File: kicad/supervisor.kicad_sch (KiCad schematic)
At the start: 63 parts, among them J1 USB-C, J2 FPGA JTAG, J51 CTRL SWD, J52 PZ254V-11-02P, SW1 CTRL BOOT, U18 CH224K, U20 SN74CB3Q3384APWR, U7 RP2350B, U8 W25Q32JVZP, Y1 12MHz ABM8-272-T3

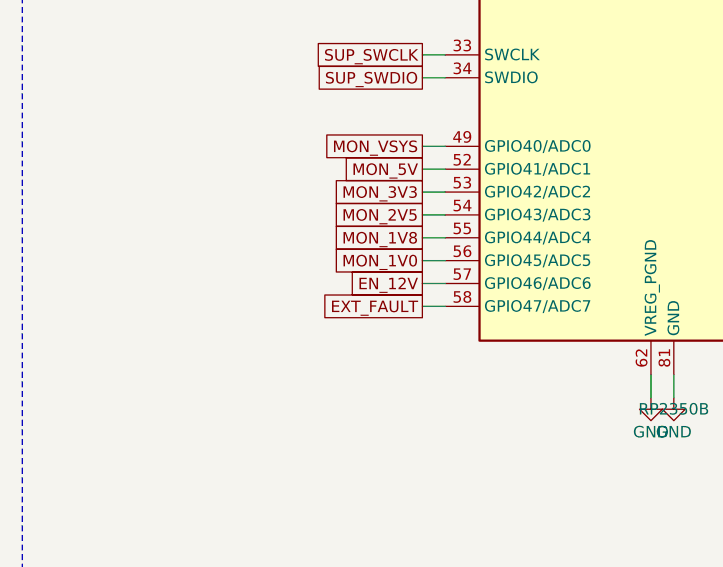
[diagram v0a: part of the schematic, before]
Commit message: Through-hole extension headers, AUX supply rework, and board state before rev A cleanup
J3/J5 become single 2x32 through-hole bodies with IO IO GND rows and a long
grounded key post per zone. Power sheet reworked around the AUX rail.
Decoupling moved off B.Cu. New footprints, 3D models and check scripts.
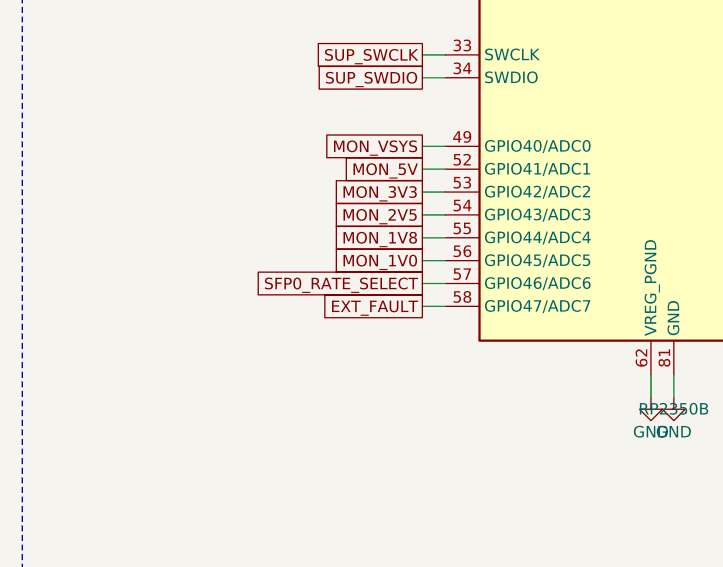
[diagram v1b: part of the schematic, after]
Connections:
- net EN_12V renamed SFP0_RATE_SELECT

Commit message: Fast Links out, Network in: RTL8211FD-CG on RGMII, ETH jack, LINK P and LINK Q
The two SFP ports, their cages, the 125 MHz oscillator, the power gate and
the I2C switch leave the design, and with them the SFP nets on the board
controller (GPIO32-39 and 46 are spare, GPIO14/31 carry the status expander's
I2C). Both GTP quads stay powered per UG482 with grounded RX and one RCAL
each.

A Network sheet replaces them: an RTL8211FD-CG gigabit PHY on RGMII at 2.5 V
with its straps, reset, interrupt, MDIO pull-up, crystal and jack LEDs wired
from the datasheet rev 1.7 tables, a HanRun HR911130A 1000Base-T magjack,
and two plain shielded 8P8C jacks that carry eight DC-coupled LVDS_25 pairs
from bank 16 with ESD arrays at the jacks. The five new parts came in through
easyeda2kicad; two footprints the importer had shared with other parts got
their own copies, and the jacks' mounting holes are NPTH.

Bank 16 moves to +2V5 and tools/alloc.py allocates it shallowest-first with
the PHY receive clock on an MRCC ball and the two link receive clocks on
clock-capable pairs; both 5 V buses and the PHY control pins live in bank 13;
banks 13, 14 and 16 are depth sorted. Escape depth >= 7 drops from 58 to 50
balls. Docs: ref/network.md and ref/link-ports.md are new; the SFP pages are
gone; status LEDs, user manual, keep-outs and import checklist follow.
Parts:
- added C182: 100nF, Capacitor_SMD:C_0402_1005Metric, symbol Device:C
- added D10, D11, D9: F.0603.00025/P2-0603G1TS2-06T-002, EasyEDA:LED0603-RD_GREEN, symbol EasyEDA:F.0603.00025_P2-0603G1TS2-06T-002
- added R128, R129, R130: 1k, Resistor_SMD:R_0402_1005Metric, symbol Device:R
- added R37, R38, R45: 4.7k, Resistor_SMD:R_0402_1005Metric, symbol Device:R
- added U17: PCF8574T_3,518, EasyEDA:SOIC-16_L10.3-W7.5-P1.27-LS10.3-BL, symbol EasyEDA:PCF8574T_3,518
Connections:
- net +3V3: now also C182.1, R128.1, R129.1, R130.1, R37.1, R38.1, R45.1, U17.16 (VDD), U17.3 (A2)
- net GND: now also C182.2, U17.1 (A0), U17.2 (A1), U17.8 (VSS)
- net SFP0_LOS: no longer names the net of U7.44 (GPIO35)
- net SFP0_MOD_ABS: no longer names the net of U7.40 (GPIO32)
- net SFP0_RATE_SELECT: no longer names the net of U7.57 (GPIO46/ADC6)
- net SFP0_TX_DIS: no longer names the net of U7.42 (GPIO33)
- net SFP0_TX_FAULT: no longer names the net of U7.43 (GPIO34)
- net SFP1_LOS: no longer names the net of U7.48 (GPIO39)
- net SFP1_MOD_ABS: no longer names the net of U7.45 (GPIO36)
- net SFP1_TX_DIS: no longer names the net of U7.46 (GPIO37)
- net SFP1_TX_FAULT: no longer names the net of U7.47 (GPIO38)
- net SFP_SCL renamed SUP_SCL
- net SUP_SCL: now also R37.2, U17.14 (SCL)
- net SFP_SDA renamed SUP_SDA
- net SUP_SDA: now also R38.2, U17.15 (SDA)
- new net CORE_1V0_GOOD: U17.7 (P3)
- new net LED_HEARTBEAT_A: D9.2 (A), R128.2
- new net LED_HEARTBEAT_N: D9.1 (C), U17.4 (P0)
- new net LED_USER1_A: D10.2 (A), R129.2
- new net LED_USER1_N: D10.1 (C), U17.5 (P1)
- new net LED_USER2_A: D11.2 (A), R130.2
- new net LED_USER2_N: D11.1 (C), U17.6 (P2)
- new net SUP_EXP_INT: R45.2, U17.13 (~{INT})
- no-connect marks 18 -> 31
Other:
- note added: "board status LEDs"
- note added: "status expander"
- moved on the sheet: C136, C137, C138, D6, D7, J1, J2, J51, J52, R11, R12, R13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

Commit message: Explain the remaining four sheets: power, memory, board controller, slots
Every part and group on the board now has its plain-words purpose, and the
gate enforces it on all six sheets. Net notes can cover a family of nets
by prefix, so regulator feedback, enables and the PSRAM series resistors
read correctly; passives credit their group's IC or connector rather than
a key post; monitor nets are no longer mistaken for supplies; parts that
are not fitted say so. PCB synced with no footprint moved.
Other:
- note added: "A small I2C chip on the board controller that drives the three status LEDs and reads the FPGA core supply's power-good signal, saving controller pins. Address 0x24. Rules for writing it: ref/status-leds.md."
- note added: "Clamps for static discharge and voltage spikes on the USB connector: D6 on the data and CC lines, D7 on the power line (VBUS)."
- note added: "Debug connector for the board controller's own processor (SWD): for developing its firmware with a debug probe. Not for the FPGA."
- note added: "Decides who programs the FPGA over JTAG. Normally (J52 open) the board controller does, through the U20 switch. Fit a jumper on J52 and U20 disconnects the board controller completely, so an external programmer plugged into J2 has the FPGA to itself. A jumper, not software, so it works even when the board controller is broken."
- note added: "Hold CTRL BOOT while plugging in USB to put the board controller in its built-in USB bootloader, for installing or recovering its firmware. The 1 k resistor lets the button win without fighting the chip. The 10 k pull-up is not fitted, as in Raspberry Pi's design."
- note added: "Negotiates the supply voltage with a USB-PD charger. The board controller tells it what to ask for (PD_CFG1-3: 5 V or 9 V, never more) and reads PD_PG to know whether the charger agreed."
- note added: "One 33 ohm resistor on every wire between the board controller and the FPGA: JTAG, the configuration pins, the FPGA flash bus, the debug sideband and the UART. They limit current if both sides ever drive the same wire at once, and damp ringing."
- note added: "Parts for the RP2350's built-in switching regulator, which makes its 1.1 V core supply (+1V1) from +3V3. Values and the inductor are the ones Raspberry Pi specifies in their hardware design guide (RP-008280 section 2.1)."
- note added: "Standard 2x5 JTAG header for an external FPGA programmer (Xilinx/AMD cable or similar). Fit J52 first."
- note added: "The board controller's 12 MHz clock: the exact crystal, load capacitors and 1 k drive-limiting resistor Raspberry Pi specifies (RP-008280 section 4)."
- note added: "The board controller's own 4 MB flash, holding its firmware. Separate from the FPGA's flash."
- note added: "The board controller's reset input. The pull-up keeps it running; the capacitor holds it in reset briefly at power-on until +3V3 is stable."
- note added: "The board controller, a Raspberry Pi RP2350B microcontroller that is always on. It is what the USB cable talks to: it loads designs into the FPGA over JTAG or writes them to the FPGA's flash, turns the supplies on in order and watches them, asks a USB-PD charger for 9 V, enables extension power, and gives the FPGA a debug and UART link. One 100 nF capacitor per supply pin (RP-008280 section 2.2.1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"
- note added: "The main connector: power in, and the USB link to your computer for programming and talking to the board."
- note added: "Three green LEDs driven by the status expander: CTRL HB blinks while the board controller firmware is alive; USER 1 and USER 2 are for software. Each has a 1 k current-limiting resistor."
- moved on the sheet: C116, C117, C118, C119, C120, C121, C122, C123, C124, C125, C126, C127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
